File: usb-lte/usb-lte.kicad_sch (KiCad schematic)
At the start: 32 parts, among them J1 Sim slot, J5 Conn_01x02_Pin, P1 USB_C_Plug_USB2.0, Q1 BC847W, Q2 BC847W, U1 AP2112K-3.3

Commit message: separate gnd and sim gnd
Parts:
- added R4: 0, Resistor_SMD:R_0402_1005Metric, symbol Device:R_Small_US
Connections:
- net GND: now also R4.2; no longer C3.2, C4.1, C5.2, C6.2, J1.5 (GND)
- new net MODEM_USIM_GND: C3.2, C4.1, C5.2, C6.2, J1.5 (GND), R4.1
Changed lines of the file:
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@@
 	(wire
 		(pts
-			(xy 194.31 59.69) (xy 194.31 57.15)
+			(xy 194.31 57.15) (xy 194.31 60.96)
 		)
 		(stroke
@@
 	(wire
 		(pts
+			(xy 194.31 66.04) (xy 194.31 67.31)
+		)
+		(stroke
+			(width 0)
+			(type default)
+		)
+	)
+	(wire
+		(pts
 			(xy 69.85 154.94) (xy 69.85 161.29)
 		)
@@
 	)
 	(symbol
+		(lib_id "power:GND")
+		(at 194.31 67.31 0)
+		(unit 1)
+		(exclude_from_sim no)
+		(in_bom yes)
+		(on_board yes)
+		(dnp no)
+		(property "Reference" "#PWR4"
+			(at 194.31 73.66 0)
+			(effects
+				(font
+					(size 1.27 1.27)
+				)
+				(hide yes)
+			)
+		)
+		(property "Value" "GND"
+			(at 194.437 71.7042 0)
+			(effects
+				(font
+					(size 1.27 1.27)
+				)
+			)
+		)
+		(property "Footprint" ""
+			(at 194.31 67.31 0)
+			(effects
+				(font
+					(size 1.27 1.27)
+				)
+				(hide yes)
+			)
+		)
+		(property "Datasheet" ""
+			(at 194.31 67.31 0)
+			(effects
+				(font
+					(size 1.27 1.27)
+				)
+				(hide yes)
+			)
+		)
+		(property "Description" ""
+			(at 194.31 67.31 0)
+			(effects
+				(font
+					(size 1.27 1.27)
+				)
+				(hide yes)
+			)
+		)
+		(pin "1"
+		)
+		(instances
+			(project "usb-lte"
+				(path "/81dea973-9ff3-499f-8a46-acefd4a76150"
+					(reference "#PWR4")
+					(unit 1)
+				)
+			)
+		)
+	)
+	(symbol
 		(lib_id "Device:R_Small_US")
 		(at 153.67 46.99 90)
@@
 	)
 	(symbol
+		(lib_id "Device:R_Small_US")
+		(at 194.31 63.5 0)
+		(unit 1)
+		(exclude_from_sim no)
+		(in_bom yes)
+		(on_board yes)
+		(dnp no)
+		(fields_autoplaced yes)
+		(property "Reference" "R4"
+			(at 196.85 62.2299 0)
+			(effects
+				(font
+					(size 1.27 1.27)
+				)
+				(justify left)
+			)
+		)
+		(property "Value" "0"
+			(at 196.85 64.7699 0)
+			(effects
+				(font
+					(size 1.27 1.27)
+				)
+				(justify left)
+			)
+		)
+		(property "Footprint" "Resistor_SMD:R_0402_1005Metric"
+			(at 194.31 63.5 0)
+			(effects
+				(font
+					(size 1.27 1.27)
+				)
+				(hide yes)
+			)
+		)
+		(property "Datasheet" "~"
+			(at 194.31 63.5 0)
+			(effects
+				(font
+					(size 1.27 1.27)
+				)
+				(hide yes)
+			)
+		)
+		(property "Description" "Resistor, small US symbol"
+			(at 194.31 63.5 0)
+			(effects
+				(font
+					(size 1.27 1.27)
+				)
+				(hide yes)
+			)
+		)
+		(pin "1"
+		)
+		(pin "2"
+		)
+		(instances
+			(project ""
+				(path "/81dea973-9ff3-499f-8a46-acefd4a76150"
+					(reference "R4")
+					(unit 1)
+				)
+			)
+		)
+	)
+	(symbol
 		(lib_id "eg95:Sim_Card_Shield_Detect")
 		(at 167.64 62.23 270)
@@
 					(unit 1)
 				)
-			)
-		)
-	)
-	(symbol
-		(lib_id "power:GND")
-		(at 194.31 59.69 0)
-		(unit 1)
-		(exclude_from_sim no)
-		(in_bom yes)
-		(on_board yes)
-		(dnp no)
-		(property "Reference" "#PWR21"
-			(at 194.31 66.04 0)
-			(effects
-				(font
-					(size 1.27 1.27)
-				)
-				(hide yes)
-			)
-		)
-		(property "Value" "GND"
-			(at 194.437 64.0842 0)
-			(effects
-				(font
-					(size 1.27 1.27)
-				)
-			)
-		)
-		(property "Footprint" ""
-			(at 194.31 59.69 0)
-			(effects
-				(font
-					(size 1.27 1.27)
-				)
-				(hide yes)
-			)
-		)
-		(property "Datasheet" ""
-			(at 194.31 59.69 0)
-			(effects
-				(font
-					(size 1.27 1.27)
-				)
-				(hide yes)
-			)
-		)
-		(property "Description" ""
-			(at 194.31 59.69 0)
-			(effects
-				(font
-					(size 1.27 1.27)
-				)
-				(hide yes)
-			)
-		)
-		(pin "1"
-		)
-		(instances
-			(project "usb-lte"
-				(path "/81dea973-9ff3-499f-8a46-acefd4a76150"
-					(reference "#PWR21")
-					(unit 1)
-				)

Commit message: Use SMPS and 3.8V for module
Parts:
- removed U1: AP2112K-3.3, Package_TO_SOT_SMD:SOT-23-5, symbol Regulator_Linear:AP2112K-3.3
- added L5: 1uH, Inductor_SMD:L_APV_ANR252012, symbol Device:L_Small
- added R13: 510k, Resistor_SMD:R_0402_1005Metric, symbol Device:R_Small_US
- added R14: 100k, Resistor_SMD:R_0402_1005Metric, symbol Device:R_Small_US
- added R15: 499k, Resistor_SMD:R_0402_1005Metric, symbol Device:R_Small_US
- added TP8, TP9: TestPoint, footprints:TestPoint_Pad_1mm, symbol Connector:TestPoint
- added U1: TPS62A02APDDC, Package_TO_SOT_SMD:SOT-563, symbol Regulator_Switching:TPS62A02ADRL
- C1: value 10uF -> 4.7uF
- C2: value 10uF -> 22uF
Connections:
- net GND: now also C2.1, R14.2, U1.1 (GND); no longer C2.2
- net VBUS: now also R9.1, TP8.1
- net at C1.1, R8.2: now also R15.2, U1.3 (VIN), U1.4 (EN)
- removed net +3V3: C2.1, R9.1
- net UART_RX_3V3 renamed UART_RX_5V
- net UART_TX_3V3 renamed UART_TX_5V
- new net: L5.1, U1.2 (SW)
- new net: R15.1, U1.6 (PG)
- new net: R13.2, R14.1, U1.5 (FB)
- new net VDD: C2.2, L5.2, R13.1, TP9.1
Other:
- note added: "5V to 3.8V"
- note added: "For VDD=3.66V, R13=510k, R14=100k For VDD=3.96V, R13=560k, R14=100k R14 must not exceed 100k"
- note removed: "5V to 3.3V"

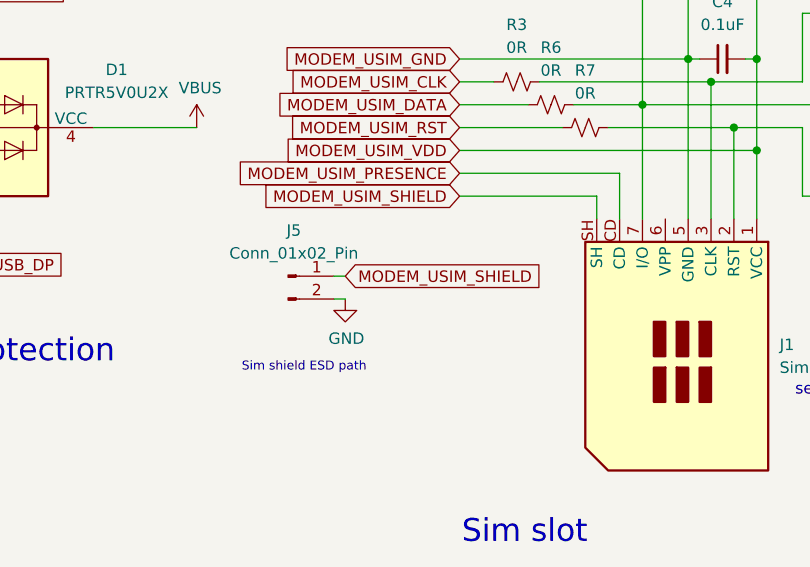
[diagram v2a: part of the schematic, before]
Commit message: Make USB C 2.0 reversible
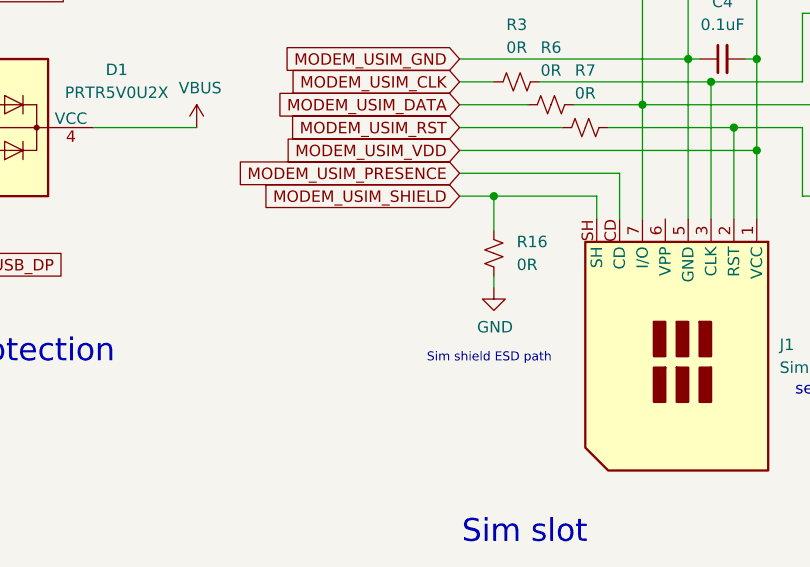
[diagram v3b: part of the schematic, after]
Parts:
- P1: footprint Expansion_Card:USB_C_Plug_Molex_105444 -> footprints:USB_C_Plug_Molex_105444
- R16: renamed from J5; value Conn_01x02_Pin -> 0R; symbol Connector:Conn_01x02_Pin -> Device:R_Small_US; now in the parts list
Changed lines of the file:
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@@
+	)
+	(junction
+		(at 147.32 57.15)
+		(diameter 0)
+		(color 0 0 0 0)
 	)
 	(junction
@@
 	(wire
 		(pts
-			(xy 130.81 68.58) (xy 129.54 68.58)
-		)
-		(stroke
-			(width 0)
-			(type default)
-		)
-	)
-	(wire
-		(pts
 			(xy 173.99 49.53) (xy 173.99 59.69)
 		)
@@
 	(wire
 		(pts
+			(xy 147.32 67.31) (xy 147.32 66.04)
+		)
+		(stroke
+			(width 0)
+			(type default)
+		)
+	)
+	(wire
+		(pts
 			(xy 181.61 49.53) (xy 173.99 49.53)
 		)
@@
 	(wire
 		(pts
+			(xy 147.32 57.15) (xy 147.32 60.96)
+		)
+		(stroke
+			(width 0)
+			(type default)
+		)
+	)
+	(wire
+		(pts
 			(xy 69.85 149.86) (xy 66.04 149.86)
 		)
@@
 	(wire
 		(pts
-			(xy 130.81 66.04) (xy 129.54 66.04)
-		)
-		(stroke
-			(width 0)
-			(type default)
-		)
-	)
-	(wire
-		(pts
 			(xy 66.04 149.86) (xy 66.04 144.78)
 		)
@@
 	(wire
 		(pts
+			(xy 147.32 57.15) (xy 158.75 57.15)
+		)
+		(stroke
+			(width 0)
+			(type default)
+		)
+	)
+	(wire
+		(pts
 			(xy 39.37 139.7) (xy 41.91 139.7)
 		)
@@
 	(wire
 		(pts
-			(xy 143.51 57.15) (xy 158.75 57.15)
+			(xy 143.51 57.15) (xy 147.32 57.15)
 		)
 		(stroke
@@
 	(text "Sim shield ESD path"
 		(exclude_from_sim no)
-		(at 126.238 76.2 0)
+		(at 146.812 75.184 0)
 		(effects
 			(font
@@
 		(property "Intersheetrefs" "${INTERSHEET_REFS}"
 			(at 278.2123 67.31 0)
-			(effects
-				(font
-					(size 1.27 1.27)
-				)
-				(justify left)
-				(hide yes)
-			)
-		)
-	)
-	(global_label "MODEM_USIM_SHIELD"
-		(shape input)
-		(at 130.81 66.04 0)
-		(fields_autoplaced yes)
-		(effects
-			(font
-				(size 1.27 1.27)
-			)
-			(justify left)
-		)
-		(property "Intersheetrefs" "${INTERSHEET_REFS}"
-			(at 153.5708 66.04 0)
 			(effects
 				(font
@@
 	(symbol
 		(lib_id "power:GND")
-		(at 130.81 68.58 0)
+		(at 147.32 67.31 0)
 		(unit 1)
 		(exclude_from_sim no)
@@
 		(dnp no)
 		(property "Reference" "#PWR30"
-			(at 130.81 74.93 0)
+			(at 147.32 73.66 0)
 			(effects
 				(font
@@
 		)
 		(property "Value" "GND"
-			(at 130.937 72.9742 0)
+			(at 147.447 71.7042 0)
 			(effects
 				(font
@@
 		)
 		(property "Footprint" ""
-			(at 130.81 68.58 0)
+			(at 147.32 67.31 0)
 			(effects
 				(font
@@
 		)
 		(property "Datasheet" ""
-			(at 130.81 68.58 0)
+			(at 147.32 67.31 0)
 			(effects
 				(font
@@
 		)
 		(property "Description" ""
-			(at 130.81 68.58 0)
+			(at 147.32 67.31 0)
 			(effects
 				(font
@@
 	)
 	(symbol
-		(lib_id "Connector:Conn_01x02_Pin")
-		(at 124.46 66.04 0)
+		(lib_id "Device:R_Small_US")
+		(at 147.32 63.5 0)
 		(unit 1)
 		(exclude_from_sim no)
-		(in_bom no)
+		(in_bom yes)
 		(on_board yes)
 		(dnp no)
 		(fields_autoplaced yes)
-		(property "Reference" "J5"
-			(at 125.095 60.96 0)
-			(effects
-				(font
-					(size 1.27 1.27)
-				)
-			)
-		)
-		(property "Value" "Conn_01x02_Pin"
-			(at 125.095 63.5 0)
-			(effects
-				(font
-					(size 1.27 1.27)
-				)
+		(property "Reference" "R16"
+			(at 149.86 62.2299 0)
+			(effects
+				(font
+					(size 1.27 1.27)
+				)
+				(justify left)
+			)
+		)
+		(property "Value" "0R"
+			(at 149.86 64.7699 0)
+			(effects
+				(font
+					(size 1.27 1.27)
+				)
+				(justify left)
 			)
 		)
 		(property "Footprint" "footprints:ESD shunt"
-			(at 124.46 66.04 0)
+			(at 147.32 63.5 0)
 			(effects
 				(font
@@
 		)
 		(property "Datasheet" "~"
-			(at 124.46 66.04 0)
-			(effects
-				(font
-					(size 1.27 1.27)
-				)
-				(hide yes)
-			)
-		)
-		(property "Description" "Generic connector, single row, 01x02, script generated"
-			(at 124.46 66.04 0)
+			(at 147.32 63.5 0)
+			(effects
+				(font
+					(size 1.27 1.27)
+				)
+				(hide yes)
+			)
+		)
+		(property "Description" "Resistor, small US symbol"
+			(at 147.32 63.5 0)
 			(effects
 				(font
@@
 			(project ""
 				(path "/81dea973-9ff3-499f-8a46-acefd4a76150"
-					(reference "J5")
+					(reference "R16")
 					(unit 1)
 				)
@@
 			)
 		)
-		(property "Footprint" "Expansion_Card:USB_C_Plug_Molex_105444"
+		(property "Footprint" "footprints:USB_C_Plug_Molex_105444"
 			(at 39.37 53.34 0)
 			(effects
@@
 			)
 		)
-		(property "Description" ""
+		(property "Description" "USB 2.0-only Type-C Plug connector"
 			(at 35.56 53.34 0)
 			(effects

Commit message: Minor changes
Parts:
- R4: value 0 -> 0R
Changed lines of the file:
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@@
 			)
 		)
-		(property "Value" "0"
+		(property "Value" "0R"
 			(at 196.85 64.7699 0)
 			(effects

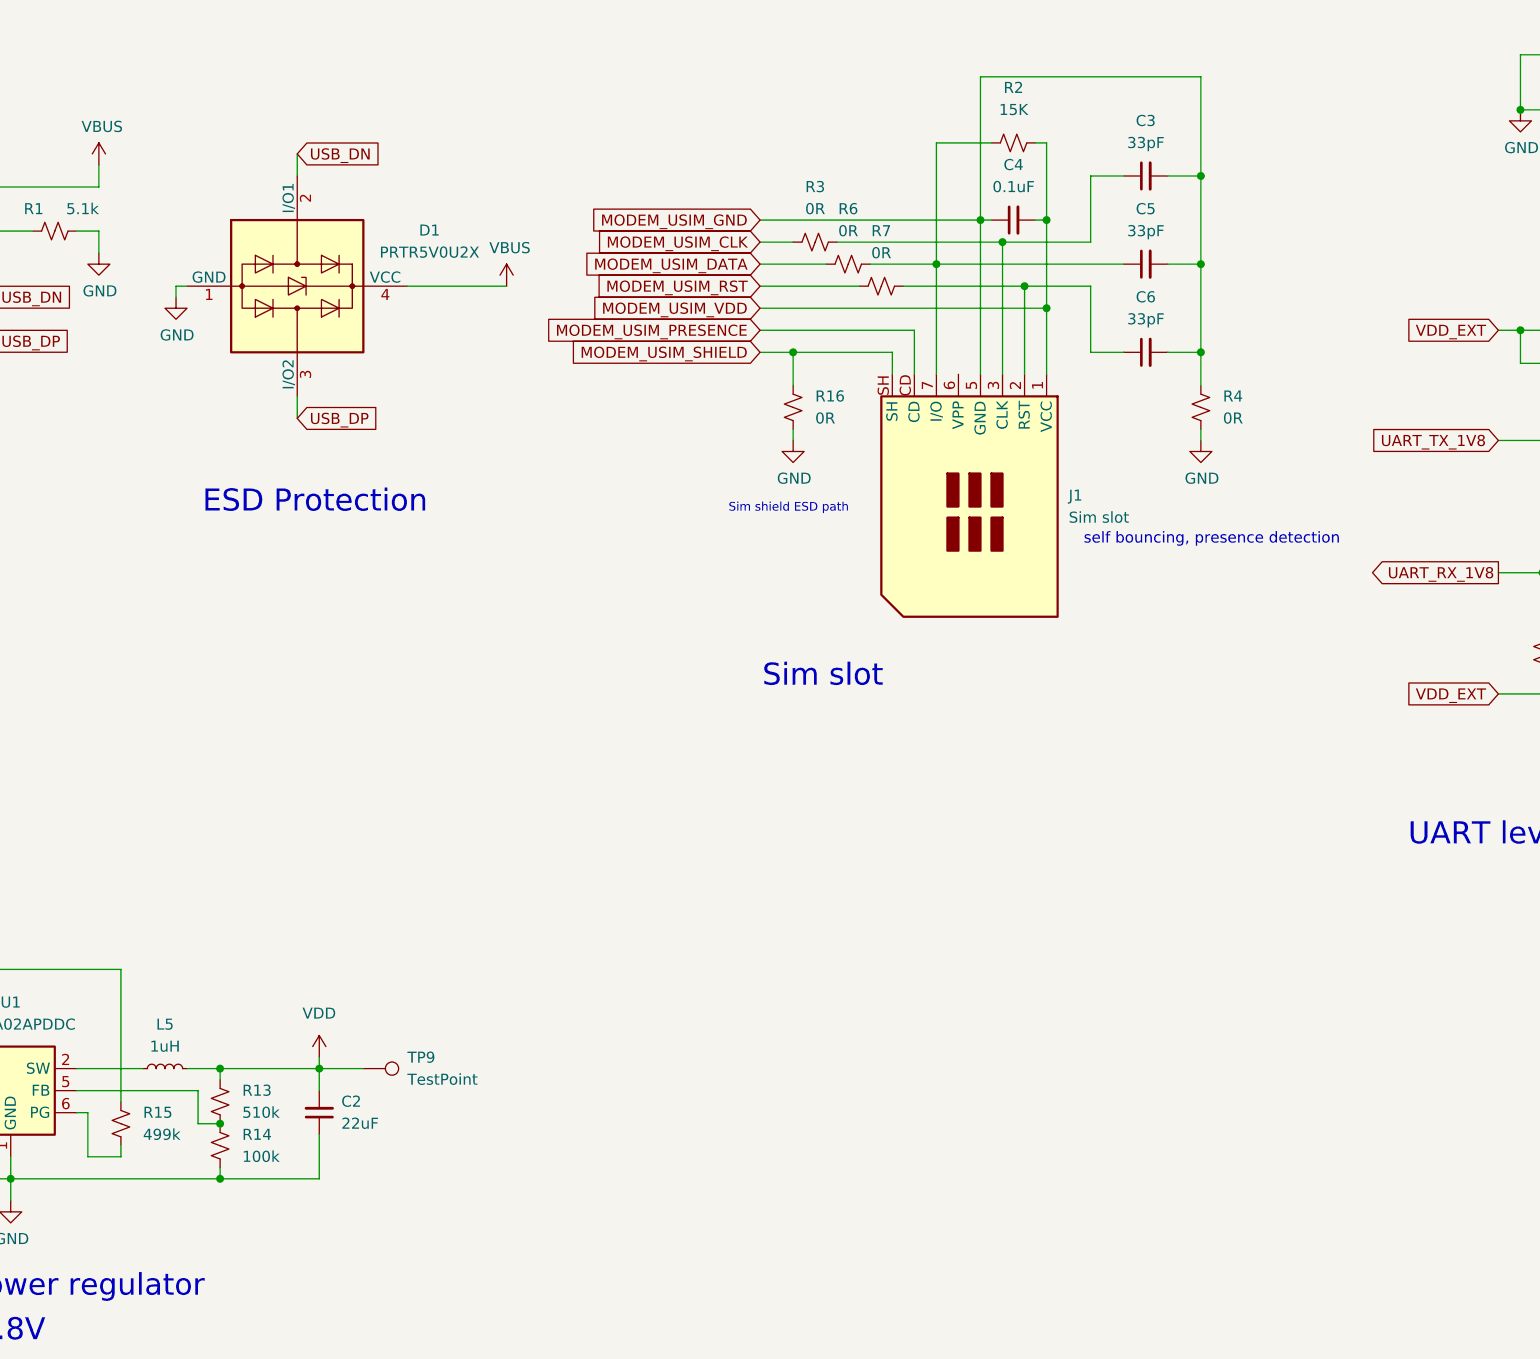
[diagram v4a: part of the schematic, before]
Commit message: Add TVS diode for sim slot
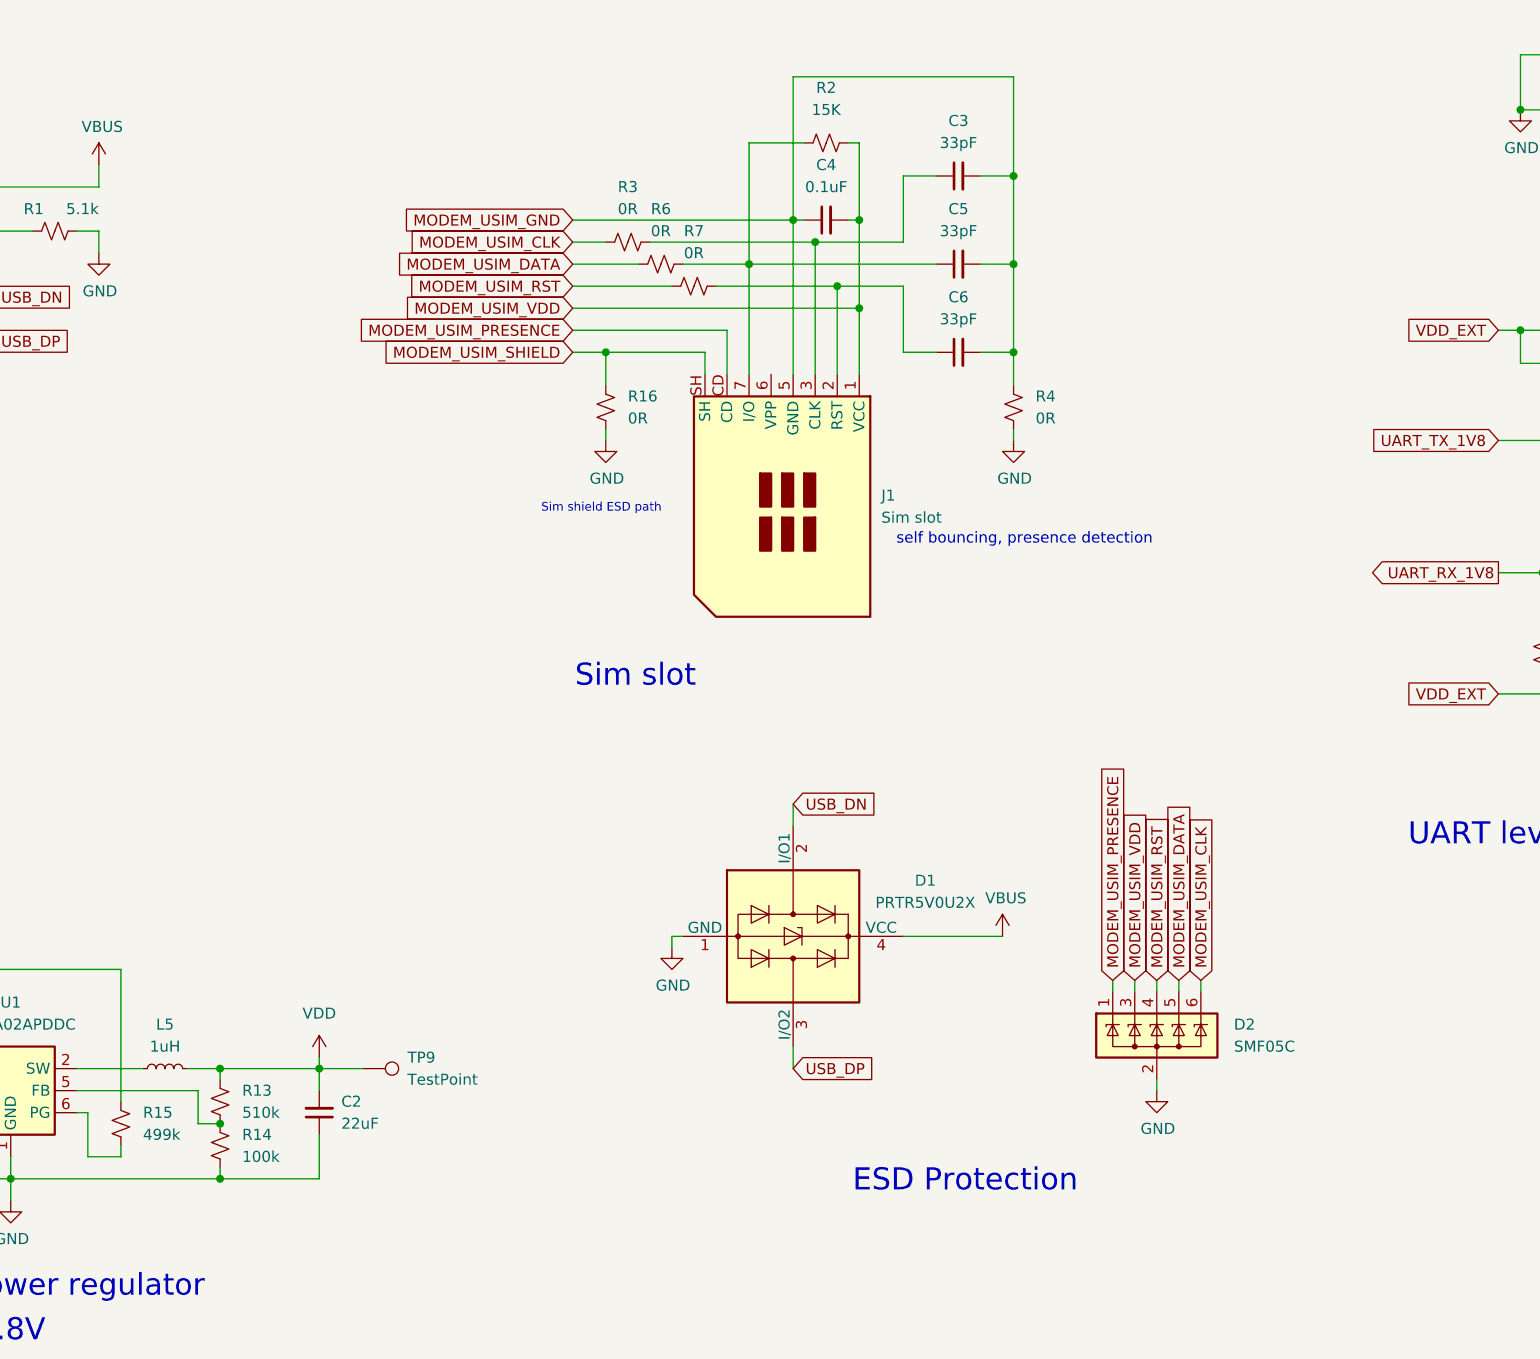
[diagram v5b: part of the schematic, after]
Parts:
- added D2: SMF05C, Package_TO_SOT_SMD:SOT-363_SC-70-6, symbol Power_Protection:SP0505BAJT
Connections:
- net GND: now also D2.2 (A)
- net MODEM_USIM_CLK: now also D2.6 (K)
- net MODEM_USIM_DATA: now also D2.5 (K)
- net MODEM_USIM_PRESENCE: now also D2.1 (K)
- net MODEM_USIM_RST: now also D2.4 (K)
- net MODEM_USIM_VDD: now also D2.3 (K)
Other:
- moved on the sheet: C3, C4, C5, C6, D1, J1, R16, R2, R3, R4, R6, R7
